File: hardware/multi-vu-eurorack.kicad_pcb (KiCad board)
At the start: 2 copper layers, 77 parts, among them IC1 LM4040DBZ-10, IC2 ATtiny85, IC3 74HC595, IC4 74HC595, J1 EURO_HEADER_10pin, J2 AVR-ISP-6, SW1 EVQQ2, U1 TLV172IDCK, U2 TL074, U3 L78L05_SOT89, U4 MCP6001-OT

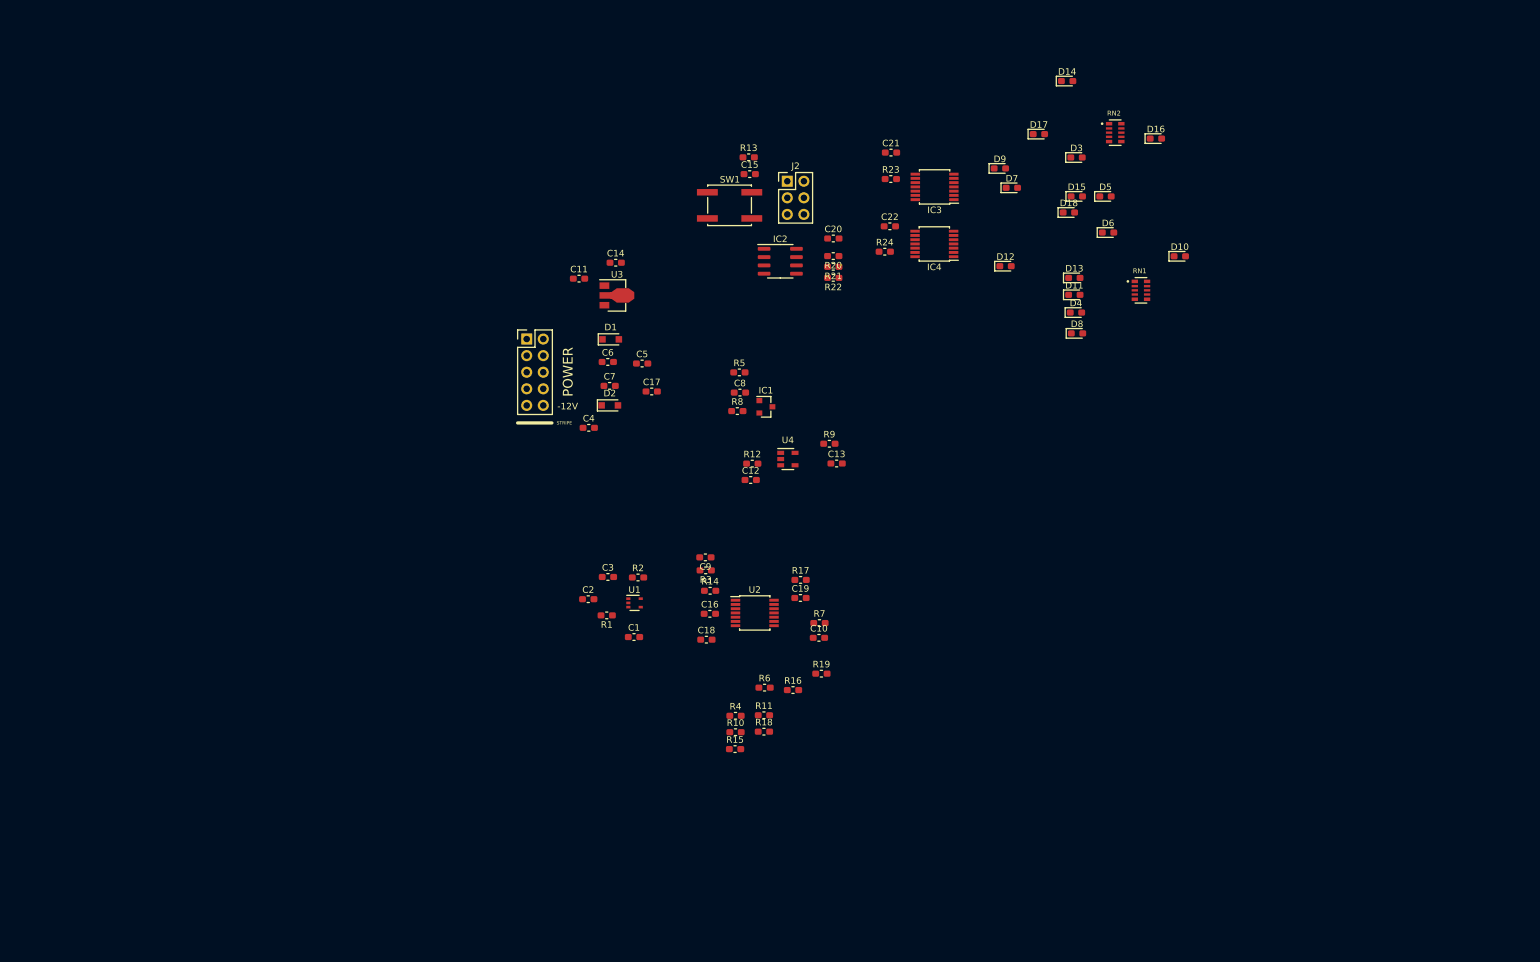
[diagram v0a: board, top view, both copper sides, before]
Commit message: Added input and output jacks and a larger array of LEDs for the main panel.
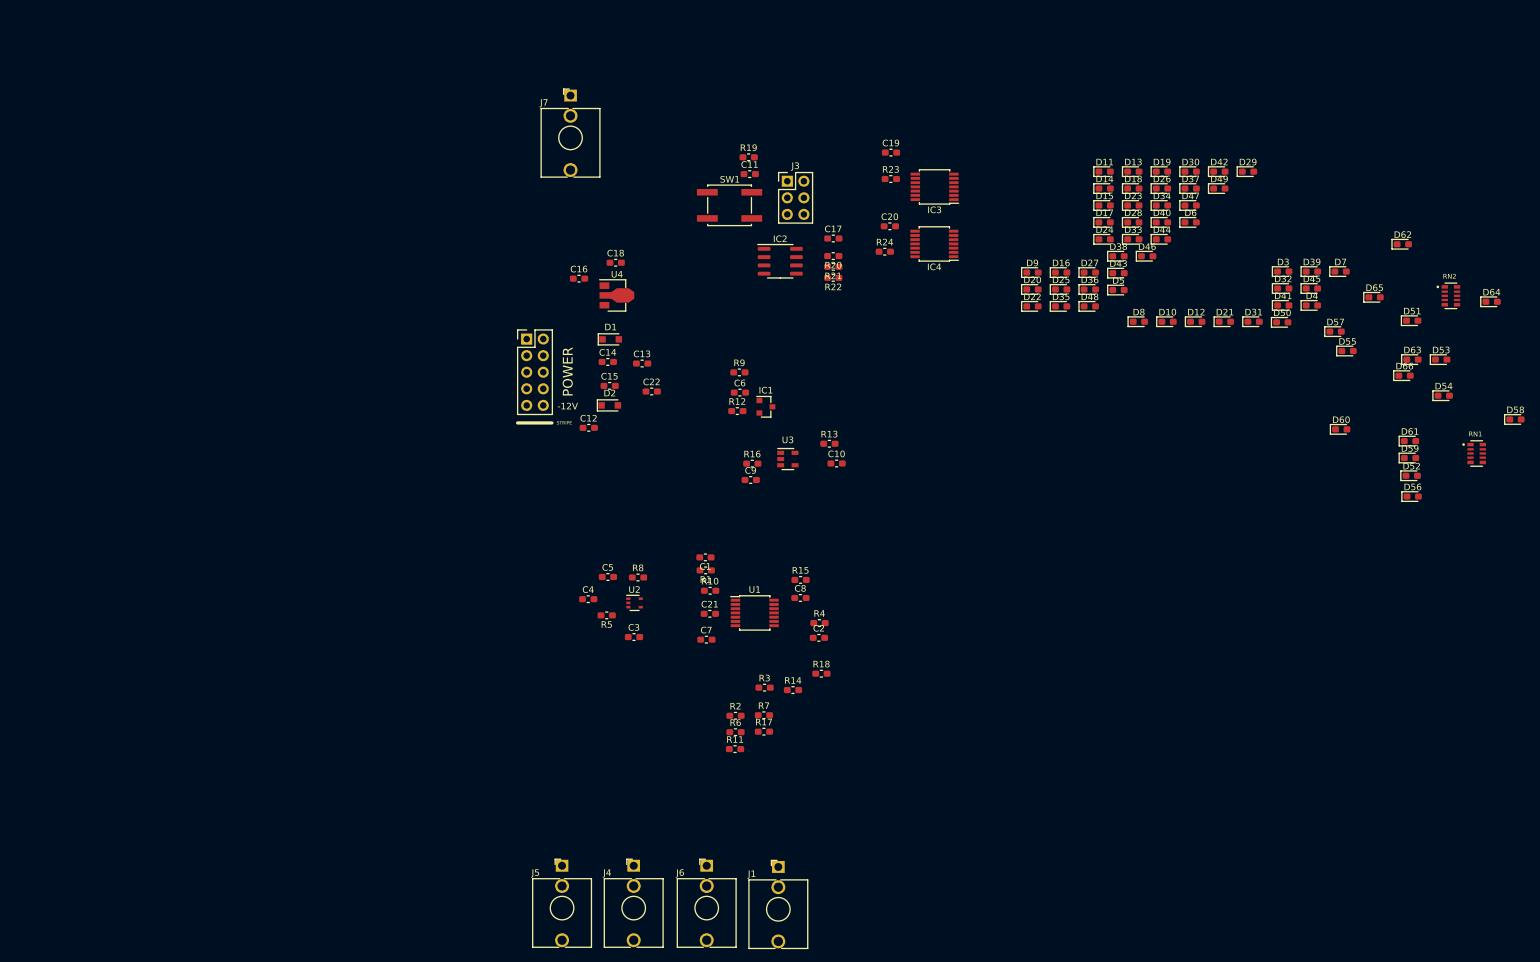
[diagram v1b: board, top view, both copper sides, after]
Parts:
- added D10: Y, LED_SMD:LED_0603_1608Metric_Pad1.05x0.95mm_HandSolder, F.Cu at (202.5, 68.0)
- added D11: G, LED_SMD:LED_0603_1608Metric_Pad1.05x0.95mm_HandSolder, F.Cu at (192.9, 45.1)
- added D12: G, LED_SMD:LED_0603_1608Metric_Pad1.05x0.95mm_HandSolder, F.Cu at (206.9, 68.0)
- added D13: G, LED_SMD:LED_0603_1608Metric_Pad1.05x0.95mm_HandSolder, F.Cu at (197.3, 45.1)
- added D14: G, LED_SMD:LED_0603_1608Metric_Pad1.05x0.95mm_HandSolder, F.Cu at (192.9, 47.6)
- added D15: G, LED_SMD:LED_0603_1608Metric_Pad1.05x0.95mm_HandSolder, F.Cu at (192.9, 50.2)
- added D16: G, LED_SMD:LED_0603_1608Metric_Pad1.05x0.95mm_HandSolder, F.Cu at (186.2, 60.5)
- added D17: B, LED_SMD:LED_0603_1608Metric_Pad1.05x0.95mm_HandSolder, F.Cu at (192.9, 52.8)
- added D18: B, LED_SMD:LED_0603_1608Metric_Pad1.05x0.95mm_HandSolder, F.Cu at (197.3, 47.6)
- added D19: R, LED_SMD:LED_0603_1608Metric_Pad1.05x0.95mm_HandSolder, F.Cu at (201.7, 45.1)
- added D20: R, LED_SMD:LED_0603_1608Metric_Pad1.05x0.95mm_HandSolder, F.Cu at (181.8, 63.1)
- added D21: A, LED_SMD:LED_0603_1608Metric_Pad1.05x0.95mm_HandSolder, F.Cu at (211.3, 68.0)
- added D22: A, LED_SMD:LED_0603_1608Metric_Pad1.05x0.95mm_HandSolder, F.Cu at (181.8, 65.7)
- added D23: A, LED_SMD:LED_0603_1608Metric_Pad1.05x0.95mm_HandSolder, F.Cu at (197.3, 50.2)
- added D24: Y, LED_SMD:LED_0603_1608Metric_Pad1.05x0.95mm_HandSolder, F.Cu at (192.9, 55.4)
- added D25: Y, LED_SMD:LED_0603_1608Metric_Pad1.05x0.95mm_HandSolder, F.Cu at (186.2, 63.1)
- added D26: Y, LED_SMD:LED_0603_1608Metric_Pad1.05x0.95mm_HandSolder, F.Cu at (201.7, 47.6)
- added D27: G, LED_SMD:LED_0603_1608Metric_Pad1.05x0.95mm_HandSolder, F.Cu at (190.6, 60.5)
- added D28: G, LED_SMD:LED_0603_1608Metric_Pad1.05x0.95mm_HandSolder, F.Cu at (197.3, 52.8)
- added D29: G, LED_SMD:LED_0603_1608Metric_Pad1.05x0.95mm_HandSolder, F.Cu at (214.8, 45.1)
- added D3: R, LED_SMD:LED_0603_1608Metric_Pad1.05x0.95mm_HandSolder, F.Cu at (220.2, 60.4)
- added D30: G, LED_SMD:LED_0603_1608Metric_Pad1.05x0.95mm_HandSolder, F.Cu at (206.0, 45.1)
- added D31: G, LED_SMD:LED_0603_1608Metric_Pad1.05x0.95mm_HandSolder, F.Cu at (215.7, 68.0)
- added D32: G, LED_SMD:LED_0603_1608Metric_Pad1.05x0.95mm_HandSolder, F.Cu at (220.2, 62.9)
- added D33: B, LED_SMD:LED_0603_1608Metric_Pad1.05x0.95mm_HandSolder, F.Cu at (197.3, 55.4)
- added D34: B, LED_SMD:LED_0603_1608Metric_Pad1.05x0.95mm_HandSolder, F.Cu at (201.7, 50.2)
- added D35: R, LED_SMD:LED_0603_1608Metric_Pad1.05x0.95mm_HandSolder, F.Cu at (186.2, 65.7)
- added D36: R, LED_SMD:LED_0603_1608Metric_Pad1.05x0.95mm_HandSolder, F.Cu at (190.6, 63.1)
- added D37: A, LED_SMD:LED_0603_1608Metric_Pad1.05x0.95mm_HandSolder, F.Cu at (206.0, 47.6)
- added D38: A, LED_SMD:LED_0603_1608Metric_Pad1.05x0.95mm_HandSolder, F.Cu at (195.0, 58.0)
- added D39: A, LED_SMD:LED_0603_1608Metric_Pad1.05x0.95mm_HandSolder, F.Cu at (224.6, 60.4)
- added D4: R, LED_SMD:LED_0603_1608Metric_Pad1.05x0.95mm_HandSolder, F.Cu at (224.6, 65.5)
- added D40: Y, LED_SMD:LED_0603_1608Metric_Pad1.05x0.95mm_HandSolder, F.Cu at (201.7, 52.8)
- added D41: Y, LED_SMD:LED_0603_1608Metric_Pad1.05x0.95mm_HandSolder, F.Cu at (220.2, 65.5)
- added D42: Y, LED_SMD:LED_0603_1608Metric_Pad1.05x0.95mm_HandSolder, F.Cu at (210.4, 45.1)
- added D43: G, LED_SMD:LED_0603_1608Metric_Pad1.05x0.95mm_HandSolder, F.Cu at (195.0, 60.6)
- added D44: G, LED_SMD:LED_0603_1608Metric_Pad1.05x0.95mm_HandSolder, F.Cu at (201.7, 55.4)
- added D45: G, LED_SMD:LED_0603_1608Metric_Pad1.05x0.95mm_HandSolder, F.Cu at (224.6, 62.9)
- added D46: G, LED_SMD:LED_0603_1608Metric_Pad1.05x0.95mm_HandSolder, F.Cu at (199.4, 58.0)
- added D47: G, LED_SMD:LED_0603_1608Metric_Pad1.05x0.95mm_HandSolder, F.Cu at (206.0, 50.2)
- added D48: G, LED_SMD:LED_0603_1608Metric_Pad1.05x0.95mm_HandSolder, F.Cu at (190.6, 65.7)
- added D49: B, LED_SMD:LED_0603_1608Metric_Pad1.05x0.95mm_HandSolder, F.Cu at (210.4, 47.6)
- added D5: A, LED_SMD:LED_0603_1608Metric_Pad1.05x0.95mm_HandSolder, F.Cu at (195.0, 63.2)
- added D50: B, LED_SMD:LED_0603_1608Metric_Pad1.05x0.95mm_HandSolder, F.Cu at (220.1, 68.1)
- added D6: A, LED_SMD:LED_0603_1608Metric_Pad1.05x0.95mm_HandSolder, F.Cu at (206.0, 52.8)
- added D7: A, LED_SMD:LED_0603_1608Metric_Pad1.05x0.95mm_HandSolder, F.Cu at (229.0, 60.4)
- added D8: Y, LED_SMD:LED_0603_1608Metric_Pad1.05x0.95mm_HandSolder, F.Cu at (198.1, 68.0)
- added D9: Y, LED_SMD:LED_0603_1608Metric_Pad1.05x0.95mm_HandSolder, F.Cu at (181.8, 60.5)
- added J1: AudioJack2_SwitchT, Connector_Audio:Jack_3.5mm_QingPu_WQP-PJ398SM_Vertical_CircularHoles, F.Cu at (142.9, 151.5)
- added J4: AudioJack2_SwitchT, Connector_Audio:Jack_3.5mm_QingPu_WQP-PJ398SM_Vertical_CircularHoles, F.Cu at (120.8, 151.3)
- added J5: AudioJack2_SwitchT, Connector_Audio:Jack_3.5mm_QingPu_WQP-PJ398SM_Vertical_CircularHoles, F.Cu at (109.8, 151.3)
- added J6: AudioJack2_SwitchT, Connector_Audio:Jack_3.5mm_QingPu_WQP-PJ398SM_Vertical_CircularHoles, F.Cu at (131.9, 151.3)
- added J7: AudioJack2_SwitchT, Connector_Audio:Jack_3.5mm_QingPu_WQP-PJ398SM_Vertical_CircularHoles, F.Cu at (111.1, 33.4)
- D51: renamed from D3; value LED_Small_ALT -> R
- D52: renamed from D4; value LED_Small_ALT -> R
- D53: renamed from D5; value LED_Small_ALT -> A
- D54: renamed from D6; value LED_Small_ALT -> A
- D55: renamed from D7; value LED_Small_ALT -> A
- D56: renamed from D8; value LED_Small_ALT -> Y
- D57: renamed from D9; value LED_Small_ALT -> Y
- D58: renamed from D10; value LED_Small_ALT -> Y
- D59: renamed from D11; value LED_Small_ALT -> G
- D60: renamed from D12; value LED_Small_ALT -> G
- D61: renamed from D13; value LED_Small_ALT -> G
- D62: renamed from D14; value LED_Small_ALT -> G
- D63: renamed from D15; value LED_Small_ALT -> G
- D64: renamed from D16; value LED_Small_ALT -> G
- D65: renamed from D17; value LED_Small_ALT -> B
- D66: renamed from D18; value LED_Small_ALT -> B
- moved D52 57.1 mm to (239.9, 91.6)
- moved D53 57.1 mm to (244.4, 73.8)
- moved D54 57.1 mm to (244.8, 79.4)
- moved D55 57.1 mm to (230.1, 72.5)
- moved D57 57.1 mm to (228.2, 69.5)
- moved D58 57.1 mm to (255.8, 83.0)
- moved D59 57.1 mm to (239.6, 88.9)
- moved D60 57.1 mm to (229.1, 84.5)
- moved D61 57.1 mm to (239.6, 86.3)
- moved D62 57.1 mm to (238.5, 56.2)
- moved D63 57.1 mm to (240.0, 73.8)
- moved D64 57.1 mm to (252.1, 65.0)
- moved D65 57.1 mm to (234.2, 64.3)
- moved D66 57.1 mm to (238.8, 76.3)
- moved RN1 57.1 mm to (249.8, 88.2)
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- renumbered C9 to C1, C13 to C10, C15 to C11, C4 to C12, C5 to C13, C6 to C14, C7 to C15, C11 to C16, C20 to C17, C14 to C18, C21 to C19, C10 to C2, C22 to C20, C16 to C21, C17 to C22, C1 to C3, C2 to C4, C3 to C5, C8 to C6, C18 to C7, C19 to C8, C12 to C9, J1 to J2, J2 to J3, R3 to R1, R14 to R10, R15 to R11, R8 to R12, R9 to R13, R16 to R14, R17 to R15, R12 to R16, R18 to R17, R19 to R18, R13 to R19, R4 to R2, R6 to R3, R7 to R4, R1 to R5, R10 to R6, R11 to R7, R2 to R8, R5 to R9, U2 to U1, U1 to U2, U4 to U3, U3 to U4
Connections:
- D51 pad 2: (no net) -> Net-(D35-Pad1)
- D52 pad 2: Net-(D4-Pad2) -> Net-(D36-Pad1)
- D53 pad 2: Net-(D5-Pad2) -> Net-(D37-Pad1)
- D54 pad 2: Net-(D6-Pad2) -> Net-(D38-Pad1)
- D55 pad 2: Net-(D7-Pad2) -> Net-(D39-Pad1)
- D56 pad 2: Net-(D8-Pad2) -> Net-(D40-Pad1)
- D57 pad 2: Net-(D9-Pad2) -> Net-(D41-Pad1)
- D58 pad 2: Net-(D10-Pad2) -> Net-(D42-Pad1)
- D59 pad 2: (no net) -> Net-(D43-Pad1)
- D60 pad 2: Net-(D12-Pad2) -> Net-(D44-Pad1)
- D61 pad 2: Net-(D13-Pad2) -> Net-(D45-Pad1)
- D62 pad 2: Net-(D14-Pad2) -> Net-(D46-Pad1)
- D63 pad 2: Net-(D15-Pad2) -> Net-(D47-Pad1)
- D64 pad 2: Net-(D16-Pad2) -> Net-(D48-Pad1)
- D65 pad 2: Net-(D17-Pad2) -> Net-(D49-Pad1)
- D66 pad 2: Net-(D18-Pad2) -> Net-(D50-Pad1)
- R17 pad 1: (no net) -> /OUTB
- R18 pad 1: (no net) -> /OUTD
- R5 pad 2: (no net) -> GND
- R6 pad 1: (no net) -> /OUTA
- R7 pad 1: (no net) -> /OUTC

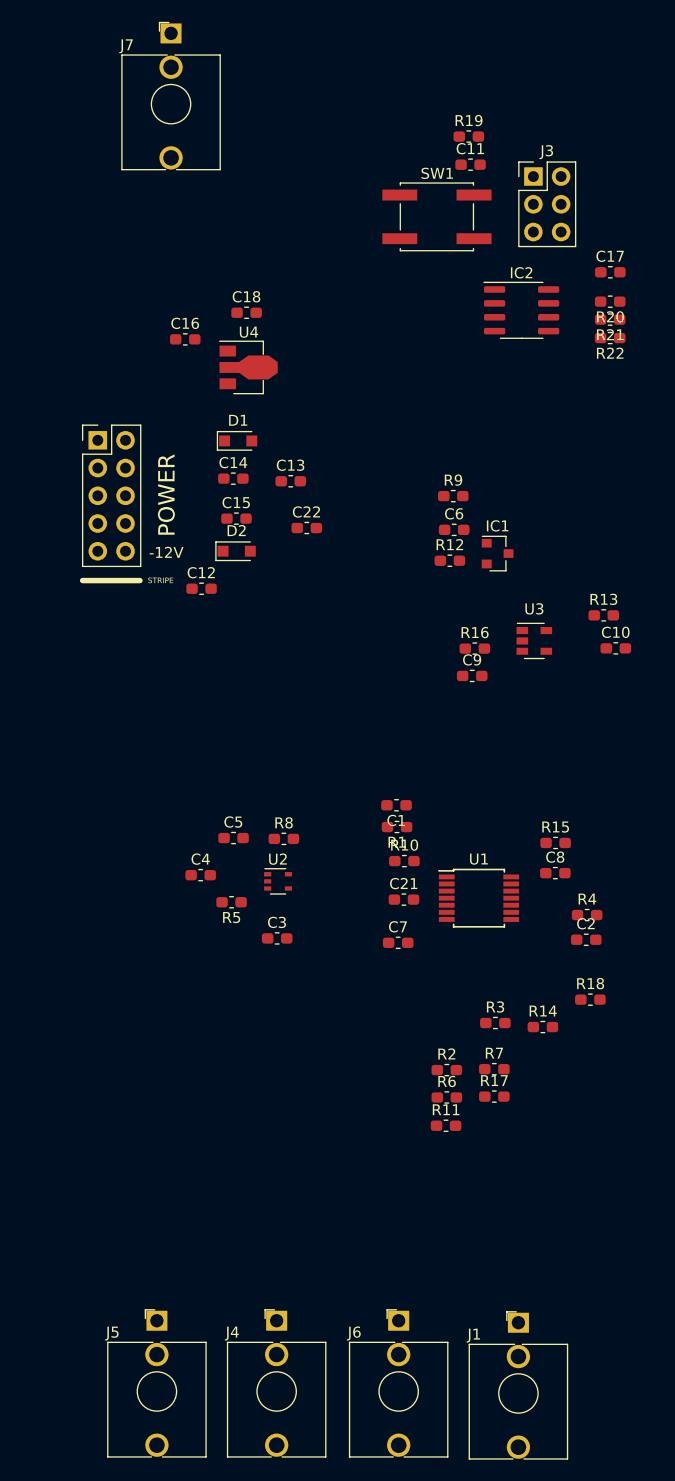
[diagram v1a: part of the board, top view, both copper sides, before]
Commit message: Updated netlist to include audio jacks. Corrected some small connection issues.
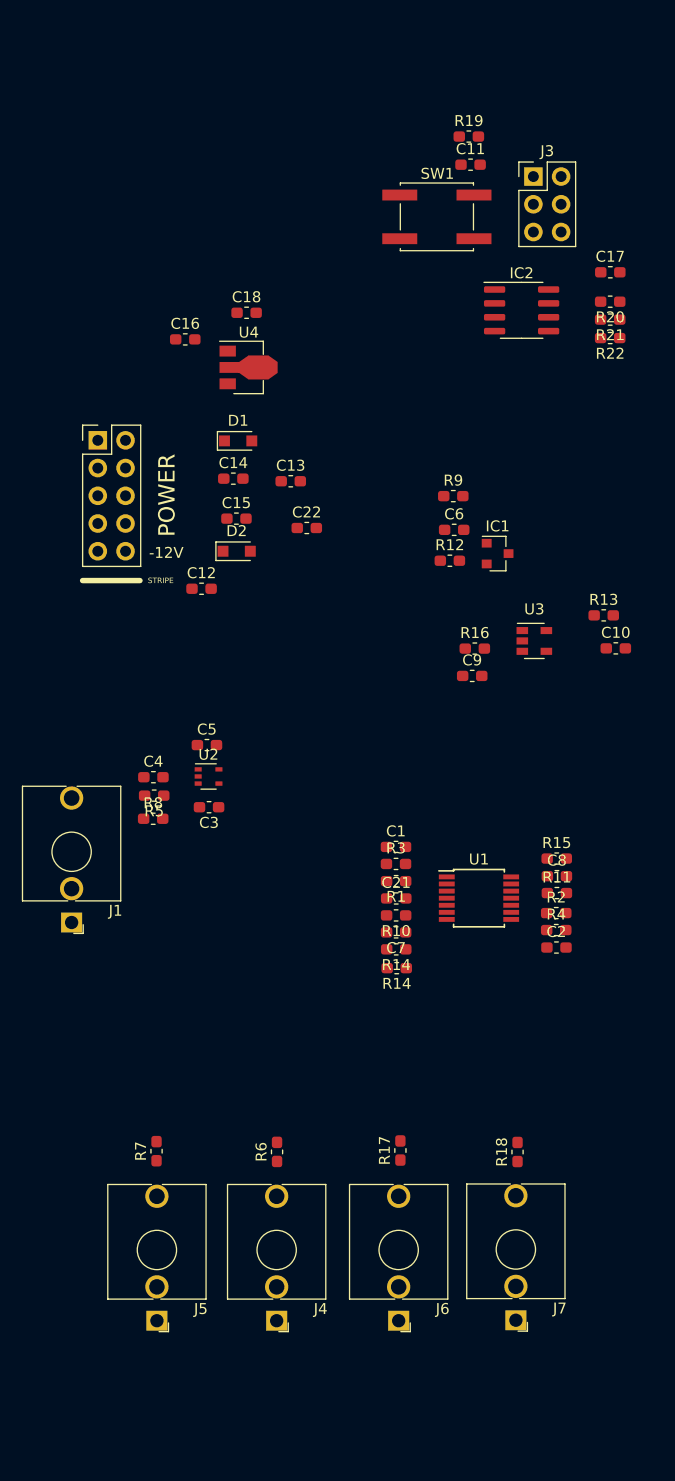
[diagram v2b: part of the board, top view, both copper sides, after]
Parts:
- added R14: 100k, Capacitor_SMD:C_0603_1608Metric_Pad1.05x0.95mm_HandSolder, F.Cu at (131.8, 119.0)
- moved J7 122.0 mm to (142.7, 151.3), turned to 180 degrees
- moved J1 54.9 mm to (102.0, 114.8), turned to 180 degrees
- moved R7 31.8 mm to (109.8, 135.8), turned to 90 degrees
- moved R11 23.6 mm to (146.4, 112.2)
- moved R2 17.5 mm to (146.4, 114.0)
- moved R3 17.2 mm to (131.7, 109.5)
- moved R6 16.3 mm to (120.8, 135.9), turned to 90 degrees
- moved R18 15.5 mm to (142.8, 135.9), turned to 90 degrees
- moved R14 15.2 mm to (131.7, 117.3), turned to 180 degrees
- moved C3 13.5 mm to (114.6, 104.3), turned to 180 degrees
- moved R8 12.1 mm to (109.5, 105.3)
- moved R5 12.1 mm to (109.6, 103.2)
- moved U2 11.5 mm to (114.5, 101.5)
- moved C4 9.96 mm to (109.5, 101.5)
- moved R17 9.92 mm to (132.1, 135.7), turned to 90 degrees
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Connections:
- J1 pad T: GND -> /INPUT
- R5 pad 2: GND -> /INPUT
